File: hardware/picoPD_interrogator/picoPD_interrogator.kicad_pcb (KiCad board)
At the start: 2 copper layers, 65.3 x 15.7 mm, 2 parts

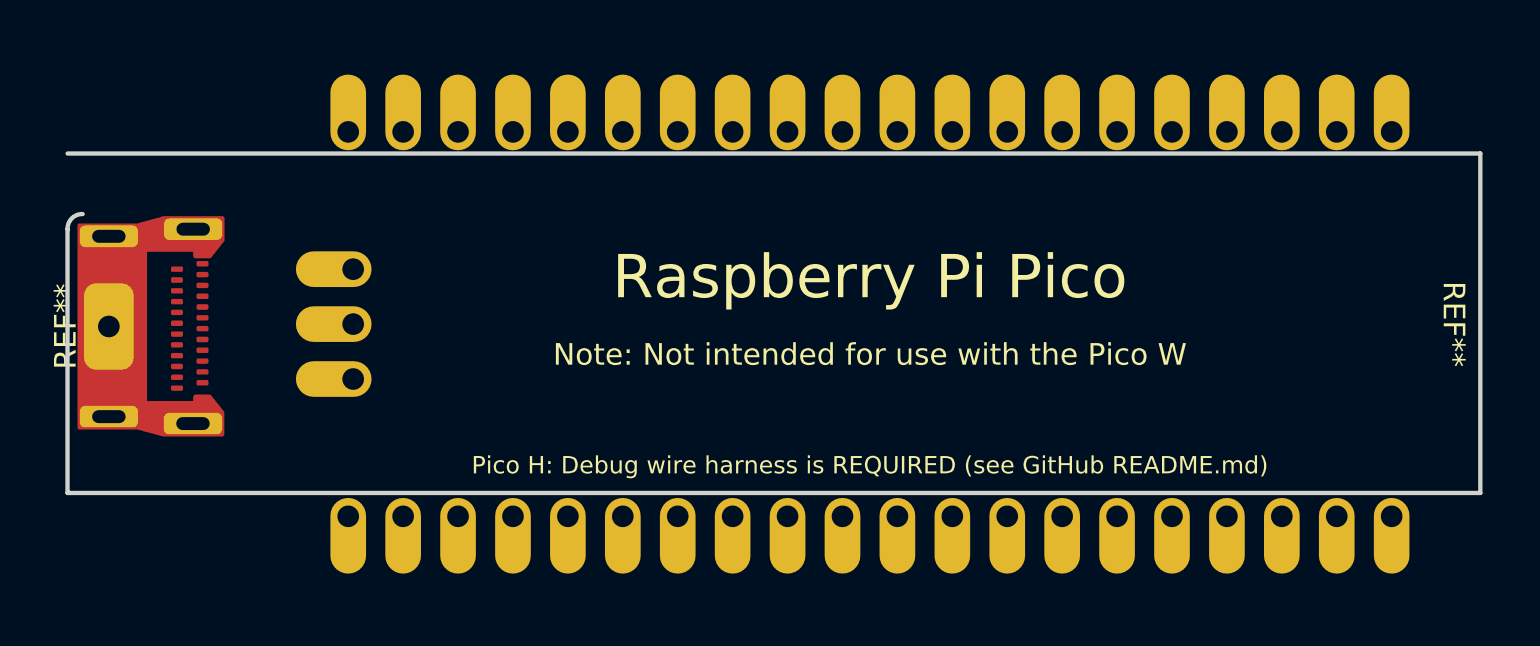
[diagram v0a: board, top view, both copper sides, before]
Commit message: Added Board Outline
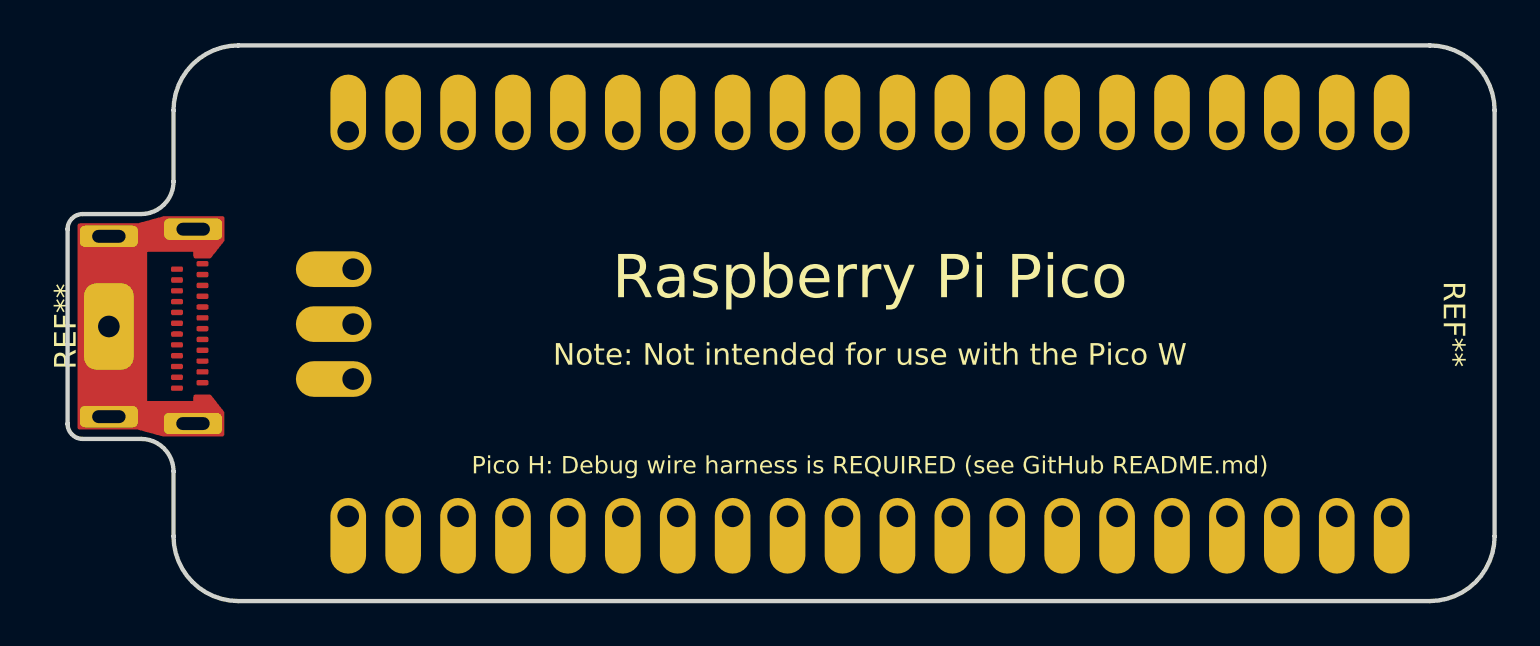
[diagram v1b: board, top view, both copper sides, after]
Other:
- board size 65.3 x 15.7 mm -> 66 x 25.7 mm
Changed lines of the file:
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@@
 		)
+	)
+	(gr_line
+		(start 120.7 93.2)
+		(end 123.4 93.2)
+		(stroke
+			(width 0.2)
+			(type default)
+		)
+		(layer "Edge.Cuts")
+	)
+	(gr_line
+		(start 124.9 81.3)
+		(end 124.9 78)
+		(stroke
+			(width 0.2)
+			(type default)
+		)
+		(layer "Edge.Cuts")
+	)
+	(gr_arc
+		(start 186 97.7)
+		(mid 185.12132 99.82132)
+		(end 183 100.7)
+		(stroke
+			(width 0.2)
+			(type default)
+		)
+		(layer "Edge.Cuts")
 	)
 	(gr_arc
 		(start 120 83.5)
-		(mid 120.198423 82.998423)
+		(mid 120.205025 83.005025)
 		(end 120.7 82.8)
 		(stroke
@@
 		(layer "Edge.Cuts")
 	)
-	(gr_line
-		(start 185.34 95.7)
-		(end 120 95.7)
+	(gr_arc
+		(start 127.9 100.7)
+		(mid 125.77868 99.82132)
+		(end 124.9 97.7)
+		(stroke
+			(width 0.2)
+			(type default)
+		)
+		(layer "Edge.Cuts")
+	)
+	(gr_arc
+		(start 183 75)
+		(mid 185.12132 75.87868)
+		(end 186 78)
 		(stroke
 			(width 0.2)
@@
 	)
 	(gr_line
-		(start 185.34 80)
-		(end 120 80)
+		(start 183 100.7)
+		(end 127.9 100.7)
 		(stroke
 			(width 0.2)
@@
 	)
 	(gr_line
-		(start 120 95.7)
+		(start 183 75)
+		(end 127.9 75)
+		(stroke
+			(width 0.2)
+			(type default)
+		)
+		(layer "Edge.Cuts")
+	)
+	(gr_line
+		(start 120 92.5)
 		(end 120 83.5)
 		(stroke
@@
 		(layer "Edge.Cuts")
 	)
-	(gr_line
-		(start 185.34 95.7)
-		(end 185.34 80)
+	(gr_arc
+		(start 124.9 78)
+		(mid 125.77868 75.87868)
+		(end 127.9 75)
 		(stroke
 			(width 0.2)
+			(type default)
+		)
+		(layer "Edge.Cuts")
+	)
+	(gr_line
+		(start 124.9 94.7)
+		(end 124.9 97.7)
+		(stroke
+			(width 0.2)
+			(type default)
+		)
+		(layer "Edge.Cuts")
+	)
+	(gr_line
+		(start 120.7 82.8)
+		(end 123.4 82.8)
+		(stroke
+			(width 0.2)
+			(type default)
+		)
+		(layer "Edge.Cuts")
+	)
+	(gr_line
+		(start 186 97.7)
+		(end 186 78)
+		(stroke
+			(width 0.2)
+			(type default)
+		)
+		(layer "Edge.Cuts")
+	)
+	(gr_arc
+		(start 124.9 81.3)
+		(mid 124.46066 82.36066)
+		(end 123.4 82.8)
+		(stroke
+			(width 0.2)
+			(type default)
+		)
+		(layer "Edge.Cuts")
+	)
+	(gr_arc
+		(start 123.4 93.2)
+		(mid 124.46066 93.63934)
+		(end 124.9 94.7)
+		(stroke
+			(width 0.2)
+			(type default)
+		)
+		(layer "Edge.Cuts")
+	)
+	(gr_arc
+		(start 120.7 93.2)
+		(mid 120.205025 92.994975)
+		(end 120 92.5)
+		(stroke
+			(width 0.2)

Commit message: Started component placement.
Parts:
- removed REF**: RaspberryPiFoundation-Pico, picoPD_interrogator:RaspberryPiFoundation-Pico
- removed REF**: USB-C_GS8, picoPD_interrogator:USB-C_GS8
- added C1: ?, Capacitor_SMD:C_0201_0603Metric, F.Cu at (82.8, 71.4)
- added C2: ?, Capacitor_SMD:C_0201_0603Metric, F.Cu at (82.8, 73.2)
- added J1: ~, picoPD_interrogator:USB-C_GS8, F.Cu at (120.4, 88.0)
- added J2: ~, picoPD_interrogator:SMD_FlipperZero_Expansion, F.Cu at (80.3, 57.6)
- added Q1: rohm-RE1C002UN, Package_TO_SOT_SMD:SOT-416, F.Cu at (79.9, 72.2)
- added Q2: rohm-RE1C002UN, Package_TO_SOT_SMD:SOT-416, F.Cu at (79.9, 75.5)
- added Q3: rohm-RE1C002UN, Package_TO_SOT_SMD:SOT-416, F.Cu at (79.9, 78.9)
- added Q4: rohm-RE1C002UN, Package_TO_SOT_SMD:SOT-416, F.Cu at (79.9, 82.2)
- added R1: 1K, Resistor_SMD:R_0201_0603Metric, F.Cu at (82.8, 74.9)
- added R10: ?, Resistor_SMD:R_0201_0603Metric, F.Cu at (85.3, 80.2)
- added R11: ?, Resistor_SMD:R_0201_0603Metric, F.Cu at (87.7, 71.4)
- added R12: 100R, Resistor_SMD:R_0201_0603Metric, F.Cu at (87.7, 73.2)
- added R13: ?, Resistor_SMD:R_0201_0603Metric, F.Cu at (87.7, 74.9)
- added R2: 3.3K, Resistor_SMD:R_0201_0603Metric, F.Cu at (82.8, 76.7)
- added R3: 0R, Resistor_SMD:R_0201_0603Metric, F.Cu at (82.8, 78.4)
- added R4: 3.3K, Resistor_SMD:R_0201_0603Metric, F.Cu at (82.8, 80.2)
- added R5: 3.3K, Resistor_SMD:R_0201_0603Metric, F.Cu at (85.3, 71.4)
- added R6: 200R, Resistor_SMD:R_0201_0603Metric, F.Cu at (85.3, 73.2)
- added R7: 100R, Resistor_SMD:R_0201_0603Metric, F.Cu at (85.3, 74.9)
- added R8: ?, Resistor_SMD:R_0201_0603Metric, F.Cu at (85.3, 76.7)
- added R9: 200R, Resistor_SMD:R_0201_0603Metric, F.Cu at (85.3, 78.4)
- added TP1: TestPoint_Flag, picoPD_interrogator:Harwin_S2751, F.Cu at (76.3, 71.8)
- added TP2: TestPoint_Flag, picoPD_interrogator:Harwin_S2751, F.Cu at (76.3, 74.2)
- added TP3: TestPoint_Flag, picoPD_interrogator:Harwin_S2751, F.Cu at (76.3, 76.7)
- added TP4: TestPoint_Flag, picoPD_interrogator:Harwin_S2751, F.Cu at (76.3, 79.1)
- added TP5: TestPoint_Flag, picoPD_interrogator:Harwin_S2751, F.Cu at (76.3, 81.5)
- added TP6: TestPoint_Flag, picoPD_interrogator:Harwin_S2751, F.Cu at (76.3, 84.0)
- added U1: ~, picoPD_interrogator:RaspberryPiFoundation-Pico, F.Cu at (157.1, 87.9)
- added U2: ST-LM393QT, picoPD_interrogator:DFN-8_2x2mm_P0.5mm_ST, F.Cu at (91.3, 72.5)

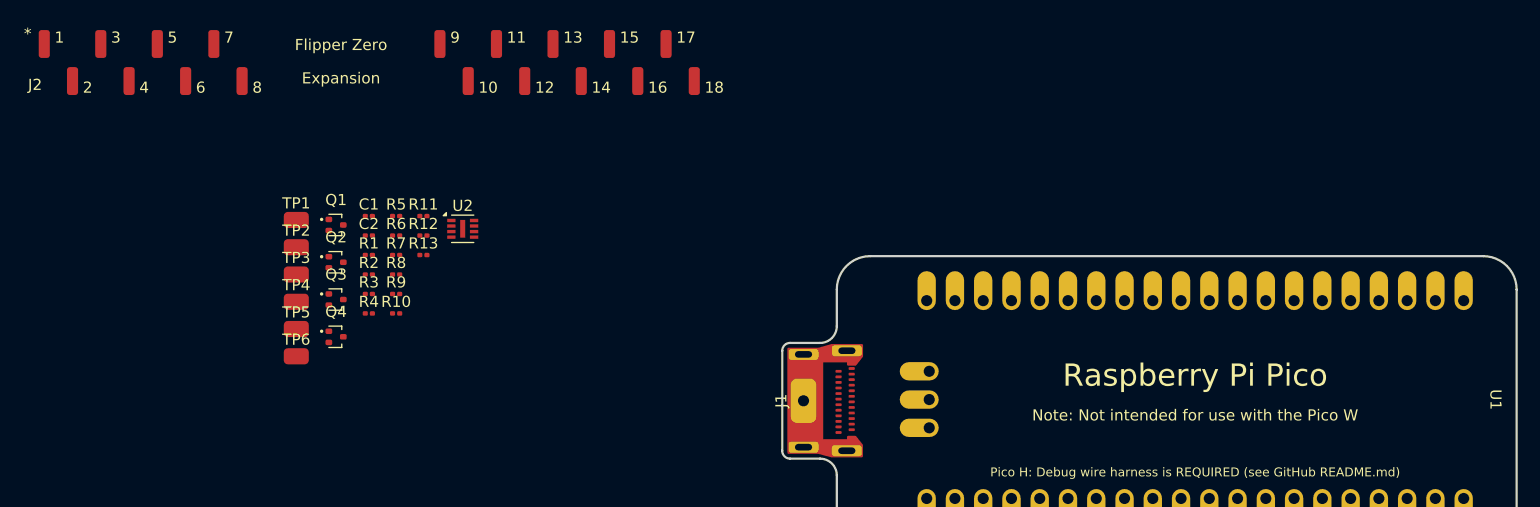
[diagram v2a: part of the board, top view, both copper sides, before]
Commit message: Fixed position of header pins connector.
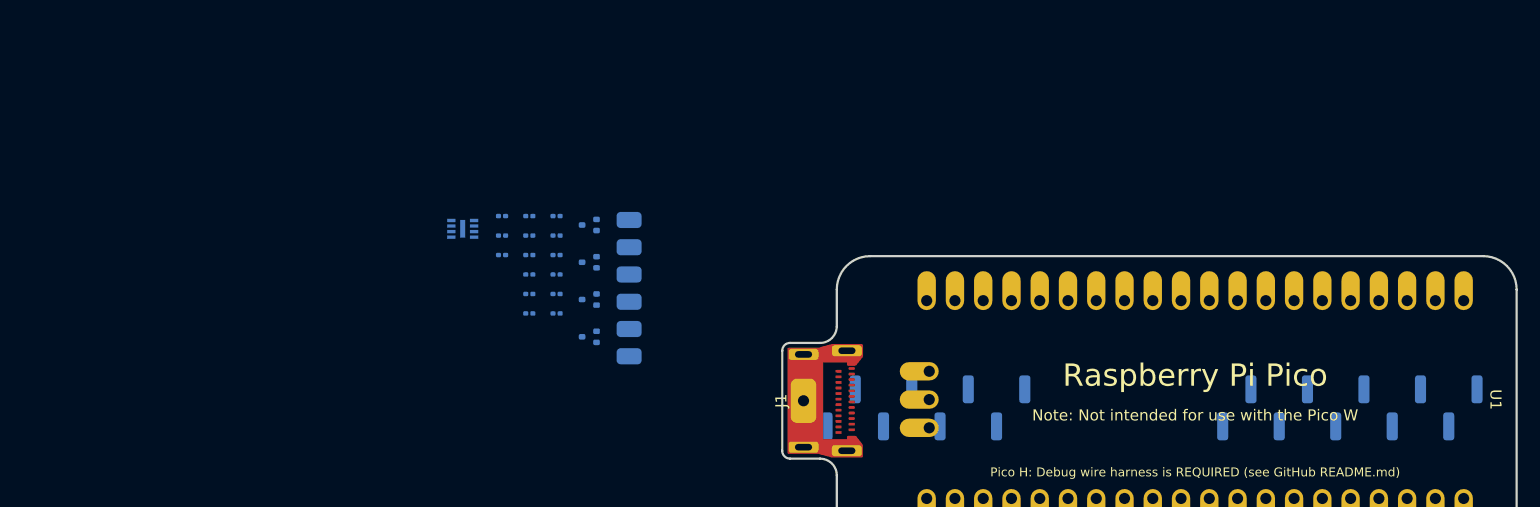
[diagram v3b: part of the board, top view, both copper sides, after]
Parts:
- C1, C2, J2, Q1, Q2, Q3, Q4, R1, R10, R11, R12, R13, R2, R3, R4, R5, R6, R7, R8, R9, TP1, TP2, TP3, TP4, TP5, TP6, U2: moved to B.Cu
- moved J2 76.9 mm to (150.7, 88.6)
- moved TP1 29.9 mm to (106.2, 71.8), turned to 180 degrees
- moved TP2 29.9 mm to (106.2, 74.2), turned to 180 degrees
- moved TP3 29.9 mm to (106.2, 76.7), turned to 180 degrees
- moved TP4 29.9 mm to (106.2, 79.1), turned to 180 degrees
- moved TP5 29.9 mm to (106.2, 81.5), turned to 180 degrees
- moved TP6 29.9 mm to (106.2, 84.0), turned to 180 degrees
- moved Q1 22.8 mm to (102.7, 72.2), turned to 180 degrees
- moved Q2 22.8 mm to (102.7, 75.5), turned to 180 degrees
- moved Q3 22.8 mm to (102.7, 78.9), turned to 180 degrees
- moved Q4 22.8 mm to (102.7, 82.2), turned to 180 degrees
- moved C1 16.9 mm to (99.7, 71.4), turned to 180 degrees
- moved C2 16.9 mm to (99.7, 73.2), turned to 180 degrees
- moved R1 16.9 mm to (99.7, 74.9), turned to 180 degrees
- moved R2 16.9 mm to (99.7, 76.7), turned to 180 degrees
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
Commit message: ...Moving things around...1
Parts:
- moved TP1 165.1 mm to (257.0, 139.1)
- moved TP2 165.1 mm to (257.0, 141.5)
- moved TP3 165.1 mm to (257.0, 143.9)
- moved TP4 165.1 mm to (257.0, 146.4)
- moved TP5 165.1 mm to (257.0, 148.8)
- moved TP6 165.1 mm to (257.0, 151.3)
- moved R12 54.2 mm to (148.4, 81.2), turned to 90 degrees
- moved Q1 53.5 mm to (152.8, 53.8)
- moved Q2 53.5 mm to (152.8, 57.1)
- moved R11 50.5 mm to (143.9, 82.9), turned to 0 degrees
- moved R13 45.8 mm to (140.2, 81.4)
- moved R9 43.9 mm to (141.1, 80.3)
- moved Q4 43.8 mm to (146.4, 81.0)
- moved C2 43.7 mm to (142.4, 82.9)
- moved Q3 41.0 mm to (143.6, 81.0)
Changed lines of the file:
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@@
 	(footprint "picoPD_interrogator:Harwin_S2751"
 		(layer "B.Cu")
-		(at 106.235 76.65 180)
+		(at 257 143.95 180)
 		(property "Reference" "TP3"
 			(at 0 1.5 0)
@@
 	(footprint "Capacitor_SMD:C_0201_0603Metric"
 		(layer "B.Cu")
-		(at 99.715 73.15 180)
+		(at 142.355 82.9 180)
 		(descr "Capacitor SMD 0201 (0603 Metric), square (rectangular) end terminal, IPC_7351 nominal, (Body size source: https://www.vishay.com/docs/20052/crcw0201e3.pdf), generated with kicad-footprint-generator")
 		(tags "capacitor")
@@
 	(footprint "Resistor_SMD:R_0201_0603Metric"
 		(layer "B.Cu")
-		(at 94.815 74.9 180)
+		(at 140.2 81.4 180)
 		(descr "Resistor SMD 0201 (0603 Metric), square (rectangular) end terminal, IPC_7351 nominal, (Body size source: https://www.vishay.com/docs/20052/crcw0201e3.pdf), generated with kicad-footprint-generator")
 		(tags "resistor")
@@
 	(footprint "Package_TO_SOT_SMD:SOT-416"
 		(layer "B.Cu")
-		(at 102.66 75.55 180)
+		(at 152.85 57.1 180)
 		(descr "SOT-416, https://www.nxp.com/docs/en/package-information/SOT416.pdf")
 		(tags "SOT-416")
@@
 	(footprint "picoPD_interrogator:Harwin_S2751"
 		(layer "B.Cu")
-		(at 106.235 74.2 180)
+		(at 257 141.5 180)
 		(property "Reference" "TP2"
 			(at 0 1.5 0)
@@
 	(footprint "picoPD_interrogator:Harwin_S2751"
 		(layer "B.Cu")
-		(at 106.235 81.55 180)
+		(at 257 148.85 180)
 		(property "Reference" "TP5"
 			(at 0 1.5 0)
@@
 	(footprint "picoPD_interrogator:Harwin_S2751"
 		(layer "B.Cu")
-		(at 106.235 71.75 180)
+		(at 257 139.05 180)
 		(property "Reference" "TP1"
 			(at 0 1.5 0)
@@
 	(footprint "picoPD_interrogator:Harwin_S2751"
 		(layer "B.Cu")
-		(at 106.235 84 180)
+		(at 257 151.3 180)
 		(property "Reference" "TP6"
 			(at 0 1.5 0)
@@
 	(footprint "Resistor_SMD:R_0201_0603Metric"
 		(layer "B.Cu")
-		(at 97.265 78.4 180)
+		(at 141.1 80.3 180)
 		(descr "Resistor SMD 0201 (0603 Metric), square (rectangular) end terminal, IPC_7351 nominal, (Body size source: https://www.vishay.com/docs/20052/crcw0201e3.pdf), generated with kicad-footprint-generator")
 		(tags "resistor")
@@
 	(footprint "Package_TO_SOT_SMD:SOT-416"
 		(layer "B.Cu")
-		(at 102.66 72.2 180)
+		(at 152.85 53.75 180)
 		(descr "SOT-416, https://www.nxp.com/docs/en/package-information/SOT416.pdf")
 		(tags "SOT-416")
@@
 	(footprint "picoPD_interrogator:Harwin_S2751"
 		(layer "B.Cu")
-		(at 106.235 79.1 180)
+		(at 257 146.4 180)
 		(property "Reference" "TP4"
 			(at 0 1.5 0)
@@
 	(footprint "Resistor_SMD:R_0201_0603Metric"
 		(layer "B.Cu")
-		(at 94.815 73.15 180)
+		(at 148.4 81.2 90)
 		(descr "Resistor SMD 0201 (0603 Metric), square (rectangular) end terminal, IPC_7351 nominal, (Body size source: https://www.vishay.com/docs/20052/crcw0201e3.pdf), generated with kicad-footprint-generator")
 		(tags "resistor")
 		(property "Reference" "R12"
-			(at 0 1.05 180)
+			(at 0 1.05 270)
 			(layer "B.SilkS")
 			(effects
@@
 		)
 		(property "Value" "100R"
-			(at 0 -1.05 180)
+			(at 0 -1.05 270)
 			(layer "B.Fab")
 			(effects
@@
 		)
 		(property "Footprint" "Resistor_SMD:R_0201_0603Metric"
-			(at 0 0 0)
+			(at 0 0 -90)
 			(unlocked yes)
 			(layer "B.Fab")
@@
 		)
 		(property "Datasheet" ""
-			(at 0 0 0)
+			(at 0 0 -90)
 			(unlocked yes)
 			(layer "B.Fab")
@@
 		)
 		(property "Description" "Resistor"
-			(at 0 0 0)
+			(at 0 0 -90)
 			(unlocked yes)
 			(layer "B.Fab")
@@
 		(attr smd)
 		(fp_line
-			(start 0.7 0.35)
-			(end -0.7 0.35)
+			(start 0.7 -0.35)
+			(end 0.7 0.35)
 			(stroke
 				(width 0.05)
@@
 		)
 		(fp_line
-			(start 0.7 -0.35)
-			(end 0.7 0.35)
+			(start -0.7 -0.35)
+			(end 0.7 -0.35)
 			(stroke
 				(width 0.05)
@@
 		)
 		(fp_line
-			(start -0.7 0.35)
-			(end -0.7 -0.35)
+			(start 0.7 0.35)
+			(end -0.7 0.35)
 			(stroke
 				(width 0.05)
@@
 		)
 		(fp_line
-			(start -0.7 -0.35)
-			(end 0.7 -0.35)
+			(start -0.7 0.35)
+			(end -0.7 -0.35)
 			(stroke
 				(width 0.05)
@@
 		)
 		(fp_line
-			(start 0.3 0.15)
-			(end -0.3 0.15)
+			(start 0.3 -0.15)
+			(end 0.3 0.15)
 			(stroke
 				(width 0.1)
@@
 		)
 		(fp_line
-			(start 0.3 -0.15)
-			(end 0.3 0.15)
+			(start -0.3 -0.15)
+			(end 0.3 -0.15)
 			(stroke
 				(width 0.1)
@@
 		)
 		(fp_line
-			(start -0.3 0.15)
-			(end -0.3 -0.15)
+			(start 0.3 0.15)
+			(end -0.3 0.15)
 			(stroke
 				(width 0.1)
@@
 		)
 		(fp_line
-			(start -0.3 -0.15)
-			(end 0.3 -0.15)
+			(start -0.3 0.15)
+			(end -0.3 -0.15)
 			(stroke
 				(width 0.1)
@@
 		)
 		(fp_text user "${REFERENCE}"
-			(at 0 0.68 180)
+			(at 0 0.68 270)
 			(layer "B.Fab")
 			(effects
@@
 		)
 		(pad "" smd roundrect
-			(at -0.345 0 180)
+			(at -0.345 0 90)
 			(size 0.318 0.36)
 			(layers "B.Paste")
@@
 		)
 		(pad "" smd roundrect
-			(at 0.345 0 180)
+			(at 0.345 0 90)
 			(size 0.318 0.36)
 			(layers "B.Paste")
@@
 		)
 		(pad "1" smd roundrect
-			(at -0.32 0 180)
+			(at -0.32 0 90)
 			(size 0.46 0.4)
 			(layers "B.Cu" "B.Mask")
@@
 		)
 		(pad "2" smd roundrect
-			(at 0.32 0 180)
+			(at 0.32 0 90)
 			(size 0.46 0.4)
 			(layers "B.Cu" "B.Mask")
@@
 	(footprint "Resistor_SMD:R_0201_0603Metric"
 		(layer "B.Cu")
-		(at 94.815 71.4 180)
+		(at 143.94 82.9)
 		(descr "Resistor SMD 0201 (0603 Metric), square (rectangular) end terminal, IPC_7351 nominal, (Body size source: https://www.vishay.com/docs/20052/crcw0201e3.pdf), generated with kicad-footprint-generator")
 		(tags "resistor")
 		(property "Reference" "R11"
-			(at 0 1.05 180)
+			(at 0 1.05 360)
 			(layer "B.SilkS")
 			(effects
@@
 		)
 		(property "Value" "?"
-			(at 0 -1.05 180)
+			(at 0 -1.05 360)
 			(layer "B.Fab")
 			(effects
@@
 		)
 		(property "Footprint" "Resistor_SMD:R_0201_0603Metric"
-			(at 0 0 0)
+			(at 0 0 180)
 			(unlocked yes)
 			(layer "B.Fab")
@@
 		)
 		(property "Datasheet" ""
-			(at 0 0 0)
+			(at 0 0 180)
 			(unlocked yes)
 			(layer "B.Fab")
@@
 		)
 		(property "Description" "Resistor"
-			(at 0 0 0)
+			(at 0 0 180)
 			(unlocked yes)
 			(layer "B.Fab")
@@
 		(attr smd)
 		(fp_line
-			(start 0.7 0.35)
-			(end -0.7 0.35)
+			(start -0.7 -0.35)
+			(end 0.7 -0.35)
 			(stroke
 				(width 0.05)
@@
 		)
 		(fp_line
-			(start 0.7 -0.35)
-			(end 0.7 0.35)
+			(start -0.7 0.35)
+			(end -0.7 -0.35)
 			(stroke
 				(width 0.05)
@@
 		)
 		(fp_line
-			(start -0.7 0.35)
-			(end -0.7 -0.35)
+			(start 0.7 -0.35)
+			(end 0.7 0.35)
 			(stroke
 				(width 0.05)
@@
 		)
 		(fp_line
-			(start -0.7 -0.35)
-			(end 0.7 -0.35)
+			(start 0.7 0.35)
+			(end -0.7 0.35)
 			(stroke
 				(width 0.05)
@@
 		)
 		(fp_line
-			(start 0.3 0.15)
-			(end -0.3 0.15)
+			(start -0.3 -0.15)
+			(end 0.3 -0.15)
 			(stroke
 				(width 0.1)
@@
 		)
 		(fp_line
-			(start 0.3 -0.15)
-			(end 0.3 0.15)
+			(start -0.3 0.15)
+			(end -0.3 -0.15)
 			(stroke
 				(width 0.1)
@@
 		)
 		(fp_line
-			(start -0.3 0.15)
-			(end -0.3 -0.15)
+			(start 0.3 -0.15)
+			(end 0.3 0.15)
 			(stroke
 				(width 0.1)
@@
 		)
 		(fp_line
-			(start -0.3 -0.15)
-			(end 0.3 -0.15)
+			(start 0.3 0.15)
+			(end -0.3 0.15)
 			(stroke
 				(width 0.1)
@@
 		)
 		(fp_text user "${REFERENCE}"
-			(at 0 0.68 180)
+			(at 0 0.68 360)
 			(layer "B.Fab")
 			(effects
@@
 		)
 		(pad "" smd roundrect
-			(at -0.345 0 180)
+			(at -0.345 0)
 			(size 0.318 0.36)
 			(layers "B.Paste")
@@
 		)
 		(pad "" smd roundrect
-			(at 0.345 0 180)
+			(at 0.345 0)
 			(size 0.318 0.36)
 			(layers "B.Paste")
@@
 		)
 		(pad "1" smd roundrect
-			(at -0.32 0 180)
+			(at -0.32 0)
 			(size 0.46 0.4)
 			(layers "B.Cu" "B.Mask")
@@
 		)
 		(pad "2" smd roundrect
-			(at 0.32 0 180)
+			(at 0.32 0)
 			(size 0.46 0.4)
 			(layers "B.Cu" "B.Mask")
@@
 	(footprint "Package_TO_SOT_SMD:SOT-416"
 		(layer "B.Cu")
-		(at 102.66 78.9 180)
+		(at 143.6 81 180)
 		(descr "SOT-416, https://www.nxp.com/docs/en/package-information/SOT416.pdf")
 		(tags "SOT-416")
@@
 	(footprint "Package_TO_SOT_SMD:SOT-416"
 		(layer "B.Cu")
-		(at 102.66 82.25 180)
+		(at 146.45 81 180)
 		(descr "SOT-416, https://www.nxp.com/docs/en/package-information/SOT416.pdf")
 		(tags "SOT-416")
